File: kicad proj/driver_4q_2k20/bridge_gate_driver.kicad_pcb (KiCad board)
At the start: 2 copper layers, 31 parts, among them M1 M210-IVERLN-1K2-24V, Q1 Transistor_NPN, Q2 FAULT RED LED, Q3 IPAN70R600P7S, Q4 IPAN70R600P7S, Q5 IPAN70R600P7S, Q6 IPAN70R600P7S, U1 DRV8701E, U2 LM555

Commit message: adicionado arquivos step, docs e footprints
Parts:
- removed Q2: FAULT RED LED, driver_4q_2k20:LTL-10224W-RED
- added C11: C, driver_4q_2k20:C_0402_1005Metric, F.Cu at (51.7, 39.1)
- added C12: C, driver_4q_2k20:C_0402_1005Metric, F.Cu at (51.9, 36.4)
- added C13: 2200uF, driver_4q_2k20:CP_Radial_D5.0mm_P2.00mm, F.Cu at (39.1, 35.4)
- added D3: 1N4001, driver_4q_2k20:D_DO-41_SOD81_P10.16mm_Horizontal, F.Cu at (48.6, 18.2)
- added D4: 1N4001, driver_4q_2k20:D_DO-41_SOD81_P10.16mm_Horizontal, F.Cu at (48.6, 23.2)
- added FAULT: FAULT RED LED, driver_4q_2k20:LTL-10224W-RED, F.Cu at (85.6, 33.4)
- added G***: LOGO, driver_4q_2k20:logo_usf, F.Cu at (22.6, 48.0)
- added R10: 619k, driver_4q_2k20:R_0402_1005Metric, F.Cu at (79.2, 35.3)
- added R11: 976k, driver_4q_2k20:R_0402_1005Metric, F.Cu at (78.7, 28.7)
- added R12: 102k, driver_4q_2k20:R_0402_1005Metric, F.Cu at (80.8, 31.8)
- added R13: 1k, driver_4q_2k20:R_0402_1005Metric, F.Cu at (80.6, 15.7)
- added R14: 1k, driver_4q_2k20:R_0402_1005Metric, F.Cu at (76.5, 19.4)
- added R15: 10k, driver_4q_2k20:R_0402_1005Metric, F.Cu at (43.6, 38.6)
- added R16: R, driver_4q_2k20:R_0402_1005Metric, F.Cu at (50.2, 41.9)
- added R17: R, driver_4q_2k20:R_0402_1005Metric, F.Cu at (51.9, 41.5)
- added R18: R, driver_4q_2k20:R_0402_1005Metric, F.Cu at (48.9, 42.0)
- added R9: 3k, driver_4q_2k20:R_0402_1005Metric, F.Cu at (75.7, 35.6)
- added T1: Transformer, driver_4q_2k20:Transformer_Breve_TEZ-28x33, F.Cu at (12.3, 17.1)
- added U3: MAX17634, driver_4q_2k20:TQFN-20-1EP_5x5mm_P0.65mm_EP3.1x3.1mm, F.Cu at (47.6, 37.5)
- added U4: AC_Con, driver_4q_2k20:395430203, F.Cu at (2.54, 19.7)
- C10: value 0.1uF -> C
- C7: value 10nF -> 0.1uF
- C8: value 0.01uF -> C
- C9: value 1uF -> C; footprint driver_4q_2k20:CP_Radial_D5.0mm_P2.00mm -> driver_4q_2k20:C_0402_1005Metric
- D1, D2: value D -> 1N4001; footprint driver_4q_2k20:S1_SMA -> driver_4q_2k20:D_DO-41_SOD81_P10.16mm_Horizontal
- M1: footprint driver_4q_2k20:Motor Connector -> driver_4q_2k20:395430203
- Q3, Q4, Q5, Q6: value IPAN70R600P7S -> FDD86580-F085; footprint driver_4q_2k20:IPAN70R600P7S -> driver_4q_2k20:TO-252-3_TabPin2
- R8: value 1k -> 12k; footprint driver_4q_2k20:C_0402_1005Metric -> driver_4q_2k20:R_0402_1005Metric
- RV1: value 5k -> 10k
- U2: value LM555 -> LTC6992_1; footprint driver_4q_2k20:TI_DGN_S-PDSO-G8 -> driver_4q_2k20:TSOT-23-6
- moved U1 71.2 mm to (80.6, 20.7), turned to 180 degrees
- moved D1 57.9 mm to (38.5, 13.0), turned to 0 degrees
- moved JP1 57.5 mm to (87.6, 43.9), turned to 180 degrees
- moved C7 48.2 mm to (75.7, 31.8), turned to 270 degrees
- moved U2 48.2 mm to (78.2, 31.8), turned to 90 degrees
- moved C2 41.8 mm to (82.9, 15.7)
- moved D2 41.5 mm to (38.5, 28.6), turned to 0 degrees
- moved R3 41.4 mm to (86.7, 26.2)
- moved R1 40.1 mm to (81.2, 17.4)
- moved C1 38.7 mm to (84.7, 21.1), turned to 270 degrees
- moved R2 38.7 mm to (85.9, 17.8), turned to 180 degrees
- moved R8 38.4 mm to (74.4, 34.3), turned to 270 degrees
- moved R7 37.7 mm to (80.4, 24.4), turned to 270 degrees
- moved RV1 37.2 mm to (78.1, 50.2)
- moved C3 36.9 mm to (82.9, 17.8), turned to 90 degrees
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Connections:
- C10 pad 1: RESET -> Net-(C10-Pad1)
- C10 pad 2: SN -> Net-(C10-Pad2)
- C2 pad 2: SN -> GND
- C3 pad 2: SN -> GND
- C5 pad 1: SN -> GND
- C6 pad 2: SN -> GND
- C7 pad 1: Net-(C7-Pad1) -> +5V
- C7 pad 2: SN -> GND
- C8 pad 1: WIPER -> Net-(C8-Pad1)
- C8 pad 2: SN -> GND
- C9 pad 1: RESET -> Net-(C9-Pad1)
- C9 pad 2: SN -> GND
- D1 pad 1: DISCH -> Net-(D1-Pad1)
- D1 pad 2: Net-(D1-Pad2) -> GND
- D2 pad 2: DISCH -> GND
- JP1 pad 1: RESET -> +5V
- JP1 pad 3: SN -> GND
- M1 pad 1: SH1 -> SH2
- M1 pad 2: SH2 -> SH1
- Q1 pad 2: SN -> GND
- R4 pad 1: SN -> GND
- R5 pad 1: RESET -> +5V
- R6 pad 2: SN -> GND
- R7 pad 2: SN -> GND
- R8 pad 1: RESET -> +5V
- R8 pad 2: DISCH -> Net-(R8-Pad2)
- RV1 pad 1: Net-(D2-Pad1) -> Net-(R8-Pad2)
- RV1 pad 2: WIPER -> MOD
- RV1 pad 3: Net-(D1-Pad2) -> GND
- U1 pad 14: DIR -> EN
- U1 pad 20: SN -> GND
- U1 pad 25: (no net) -> GND
- U1 pad 5: SN -> GND
- U2 pad 1: SN -> MOD
- U2 pad 2: WIPER -> GND
- U2 pad 3: DIR -> Net-(R10-Pad1)
- U2 pad 4: RESET -> Net-(R11-Pad2)
- U2 pad 5: Net-(C7-Pad1) -> +5V
- U2 pad 6: WIPER -> EN
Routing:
- net +24V: track 0.00 -> 67.7 mm
- net WIPER: track 59.8 -> 0.00 mm
- net Net-(C12-Pad1): track 0.00 -> 49.4 mm
- net SH2: track 0.00 -> 45.9 mm, vias 0 -> 2
- net +5V: track 0.00 -> 36.3 mm
- net SP: track 0.00 -> 35.1 mm, vias 0 -> 3
- net GL2: track 0.00 -> 32.9 mm, vias 0 -> 2
- net SH1: track 0.00 -> 32.5 mm, vias 0 -> 2
- net GH2: track 0.00 -> 31.0 mm, vias 0 -> 3
- net SN: track 29.5 -> 0.00 mm
- net DIR: track 21.8 -> 48.5 mm, vias 0 -> 4
- net RESET: track 22.9 -> 0.00 mm
- net Net-(T1-Pad5): track 0.00 -> 22.3 mm
- net GL1: track 0.00 -> 21.6 mm, vias 0 -> 2
- net MOD: track 0.00 -> 17.4 mm
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- added copper zone on B.Cu, net GND
- added copper zone on F.Cu, net GND
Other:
- board outline added: 97 x 43 mm
- net class Default: via_drill 0.4 -> 0.15
- net class Logic Signal added: clearance 0.2, trace_width 0.2, via_dia 0.8, via_drill 0.4
- net class Motor added: clearance 0.2, trace_width 2.03286, via_dia 0.8, via_drill 0.4
- rule via_min_drill: 0.3 -> 0.15
- rule via_min_size: 0.4 -> 0.2
- board text added: "24V 3.2A"
- board text added: "CCW"
- board text added: "CW"
- board text added: "ELETRÔNICA DE POTÊNCIA"

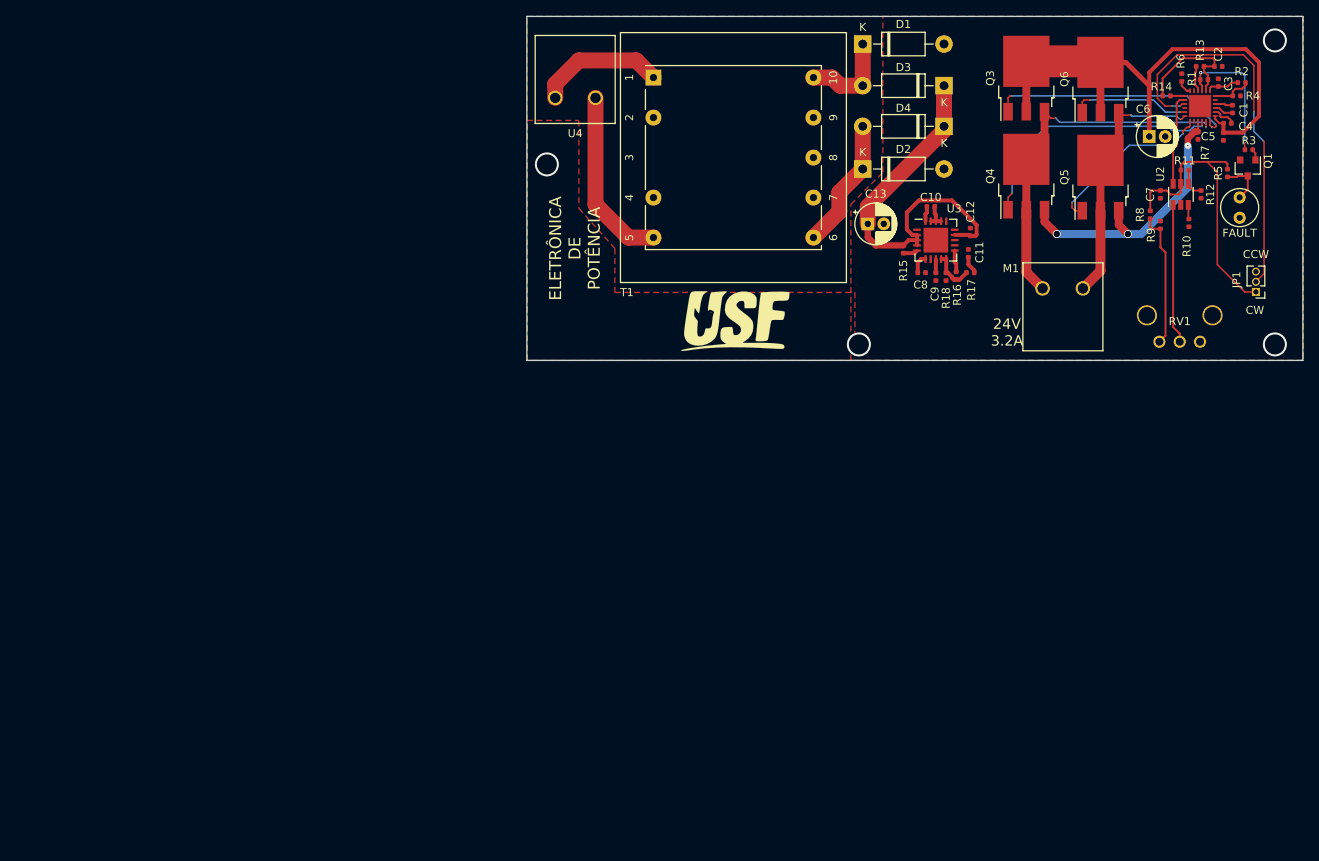
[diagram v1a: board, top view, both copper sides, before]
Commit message: added power supply and new transformer
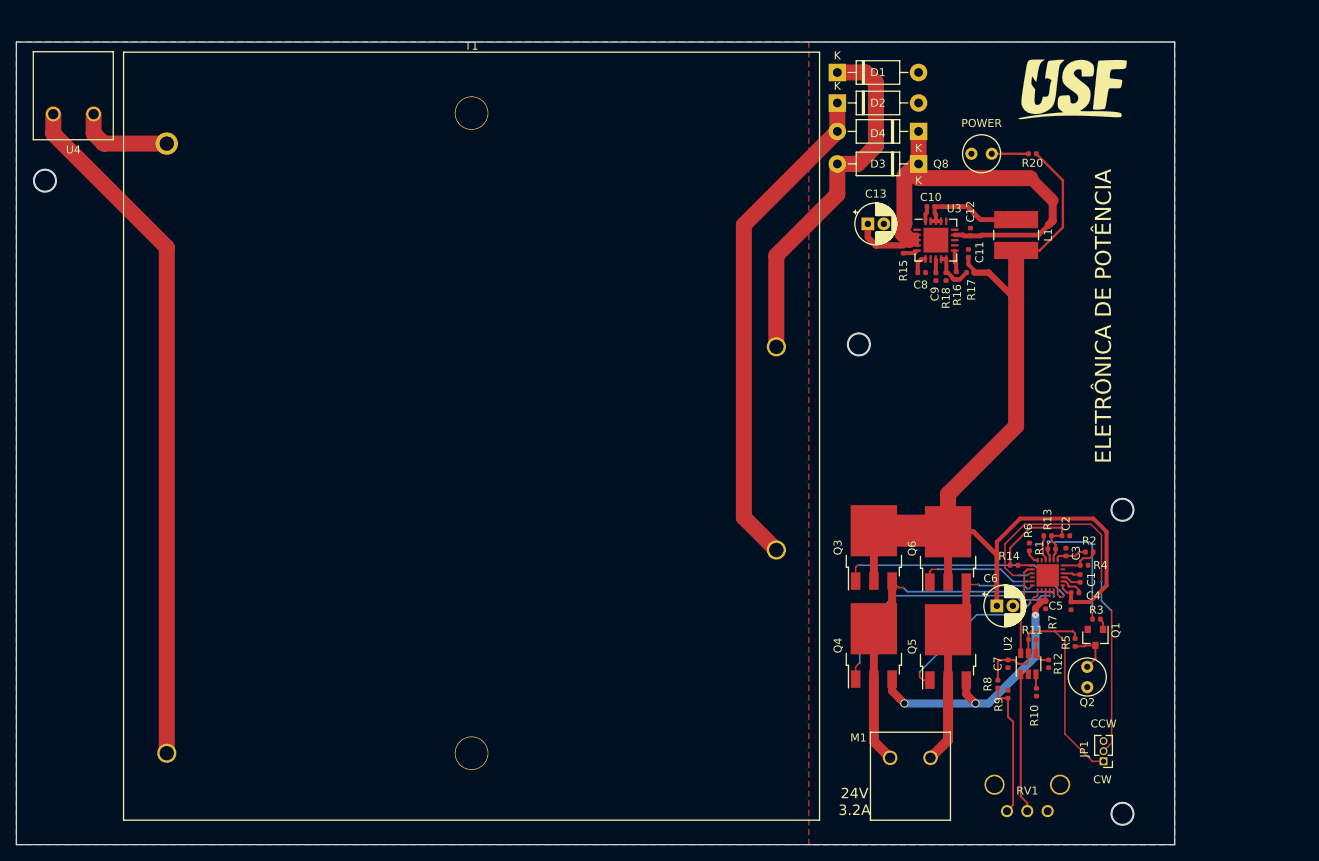
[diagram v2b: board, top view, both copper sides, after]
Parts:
- added L1: 7.5uH, driver_4q_2k20:L_TracoPower_TCK-047_5.2x5.8mm, F.Cu at (57.7, 36.8)
- added Q8: FAULT RED LED, driver_4q_2k20:LTL-10224W-RED, F.Cu at (53.3, 26.7)
- added R20: 710, driver_4q_2k20:C_0402_1005Metric, F.Cu at (59.7, 26.7)
- C10: value C -> 0.1uF
- C11: value C -> 3.2uF
- C12: value C -> 0.18uF
- C8: value C -> 2.2uF
- C9: value C -> 4300pF
- D1, D2, D3, D4: value 1N4001 -> MUR410
- R16: value R -> 8.06k
- R17: value R -> 620k
- R18: value R -> 24k
- T1: value Transformer -> Transformer_V2; footprint driver_4q_2k20:Transformer_Breve_TEZ-28x33 -> driver_4q_2k20:Transformer_96x87
- U3: value MAX17634 -> MAX17634C
- moved U4 62.8 mm to (-60.2, 21.7)
- moved C6 61.7 mm to (55.2, 83.2)
- moved R10 61.7 mm to (60.2, 94.0)
- moved R12 61.7 mm to (61.7, 90.4)
- moved R7 61.7 mm to (61.3, 83.1)
- moved Q1 61.7 mm to (67.6, 87.1)
- moved RV1 61.7 mm to (59.1, 108.8)
- moved C4 61.7 mm to (65.0, 81.5)
- moved C5 61.7 mm to (64.5, 83.2)
- moved C7 61.7 mm to (56.6, 90.4)
- moved M1 61.7 mm to (44.5, 102.2)
- moved Q4 61.7 mm to (39.9, 88.1)
- moved R1 61.7 mm to (62.1, 76.1)
- moved R11 61.7 mm to (59.7, 87.4)
- moved R14 61.7 mm to (57.4, 78.1)
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- renumbered FAULT to Q2
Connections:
- C4 pad 2: +24V -> 24V
- C5 pad 2: +24V -> 24V
- C6 pad 1: +24V -> 24V
- Q3 pad 2: +24V -> 24V
- Q6 pad 2: +24V -> 24V
- T1 pad 2: (no net) -> Net-(T1-Pad2)
- T1 pad 4: (no net) -> Net-(D2-Pad1)
- T1 pad 5: Net-(T1-Pad5) -> (no net)
- U1 pad 1: +24V -> 24V
- U1 pad 25: GND -> (no net)
- U4 pad 1: Net-(T1-Pad5) -> Net-(T1-Pad1)
- U4 pad 2: Net-(T1-Pad1) -> Net-(T1-Pad2)
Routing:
- net 24V: track 2.23 -> 132.7 mm
- net Net-(T1-Pad2): track 0.00 -> 85.8 mm
- net +24V: track 67.7 -> 0.00 mm
- net Net-(D2-Pad1): track 16.5 -> 62.4 mm
- net Net-(D1-Pad1): track 11.8 -> 45.0 mm
- net Net-(T1-Pad5): track 22.3 -> 0.00 mm
- net Net-(C12-Pad1): track 49.4 -> 68.9 mm
- net Net-(C10-Pad2): track 3.14 -> 14.0 mm
- net Net-(Q8-Pad1): track 0.00 -> 4.59 mm
- net Net-(T1-Pad1): track 16.1 -> 12.1 mm
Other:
- board size 97 x 43 mm -> 144.8 x 100.3 mm
- board text added: "POWER"
